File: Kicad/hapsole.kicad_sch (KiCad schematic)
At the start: 52 parts, among them J1 USB_C_Receptacle_USB2.0_16P, J2 Conn_01x02_Socket, J3 Conn_01x02_Socket, Q1 PMOS, U1 DA7280-00V42, U2 DA7280-00V42, U3 nRF52840, U4 LSM6DS3TR-C, U5 BQ25100YFPR, U6 TLV73333PDBV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

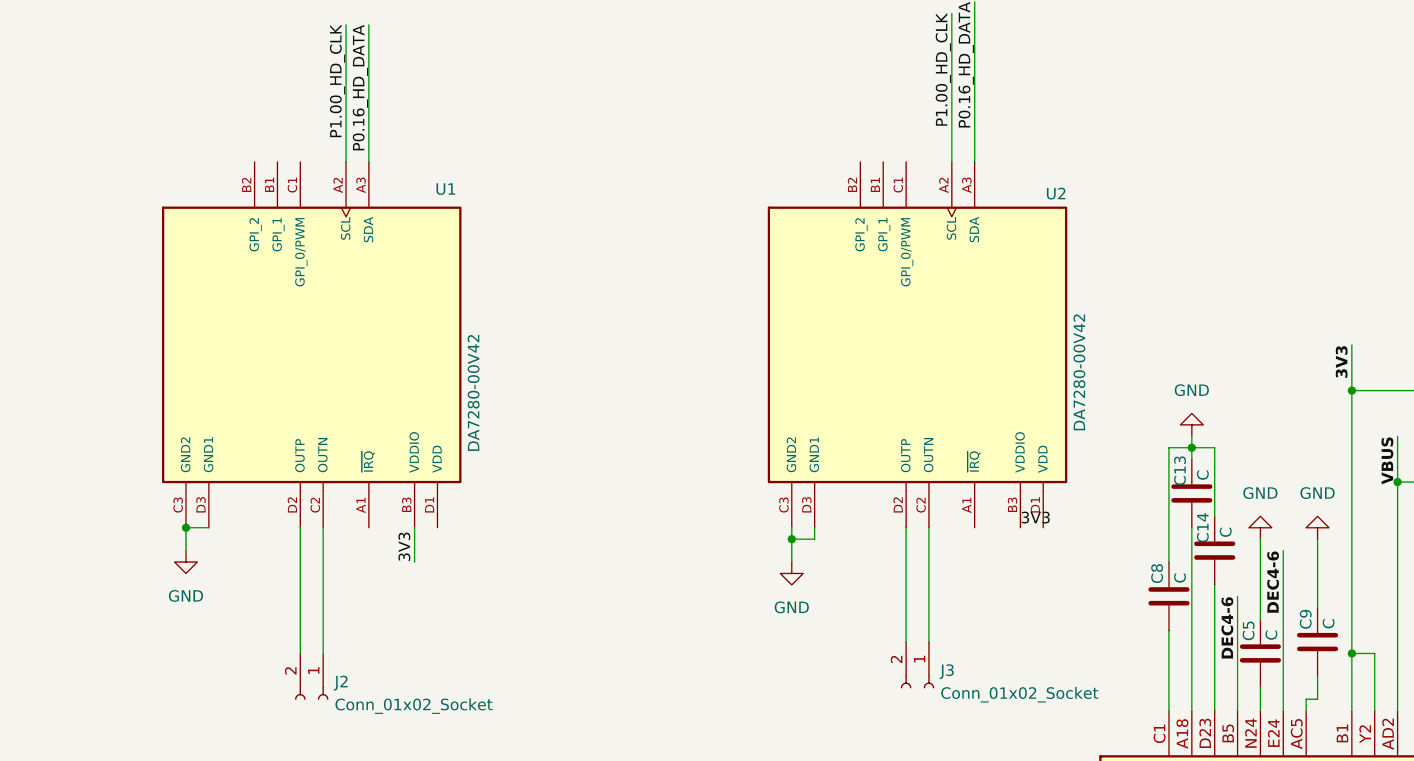
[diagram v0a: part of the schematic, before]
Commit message: added da7281
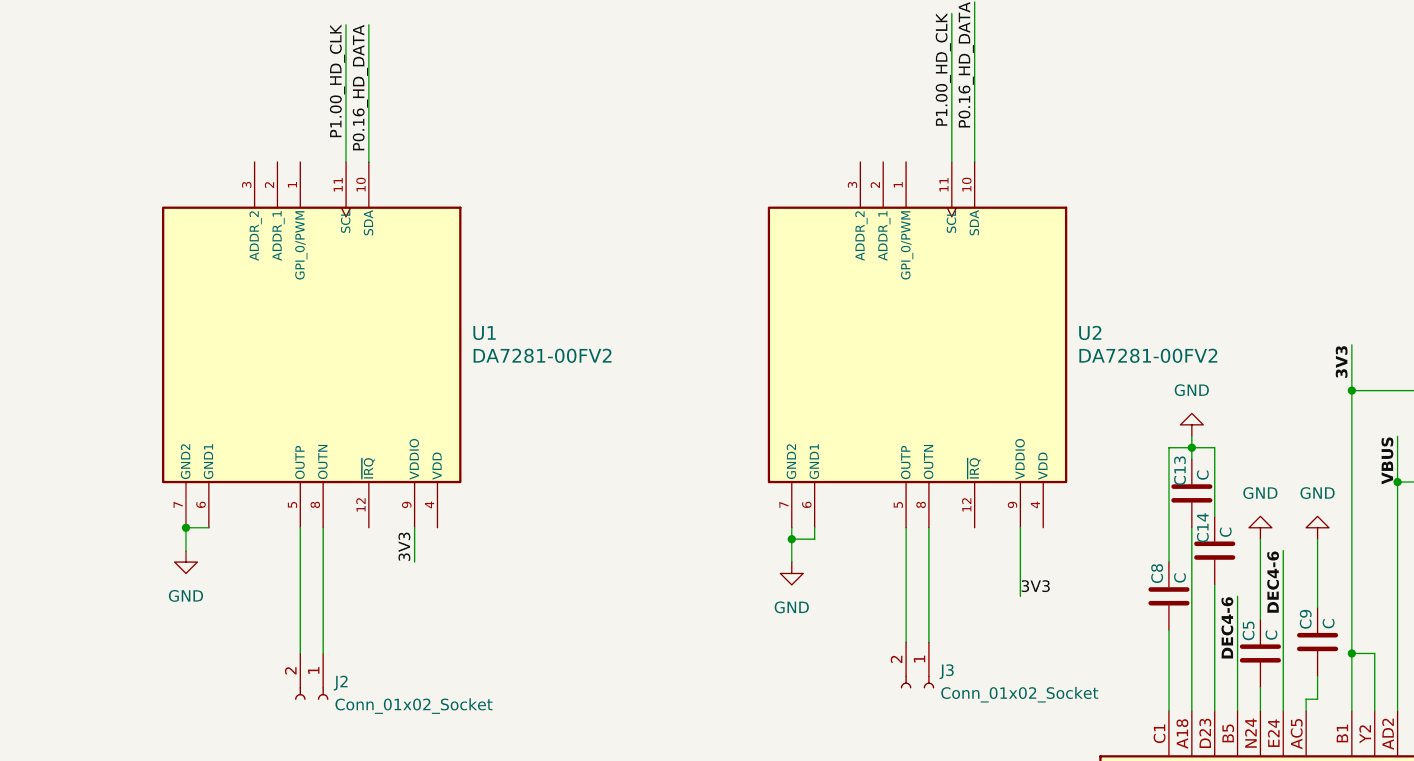
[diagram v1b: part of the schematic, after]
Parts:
- removed U1, U2: DA7280-00V42, DA7280-00V42:BGA12N40P4X3_175X135X57, symbol Arjun_Custom:DA7280-00V42
- added U1, U2: DA7281-00FV2, DA7281-00FV2_DIL, symbol Arjun_Custom:DA7281-00FV2
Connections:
- net 3V3: now also U1.9 (VDDIO), U2.9 (VDDIO)
- net GND: now also U1.6 (GND1), U1.7 (GND2), U2.6 (GND1), U2.7 (GND2)
- net P0.16_HD_DATA: now also U1.10 (SDA), U2.10 (SDA)
- net P1.00_HD_CLK: now also U1.11 (SCL), U2.11 (SCL)
- net at J3.1 (Pin_1): now also U2.8 (OUTN)
- net at J3.2 (Pin_2): now also U2.5 (OUTP)
- net at J2.1 (Pin_1): now also U1.8 (OUTN)
- net at J2.2 (Pin_2): now also U1.5 (OUTP)

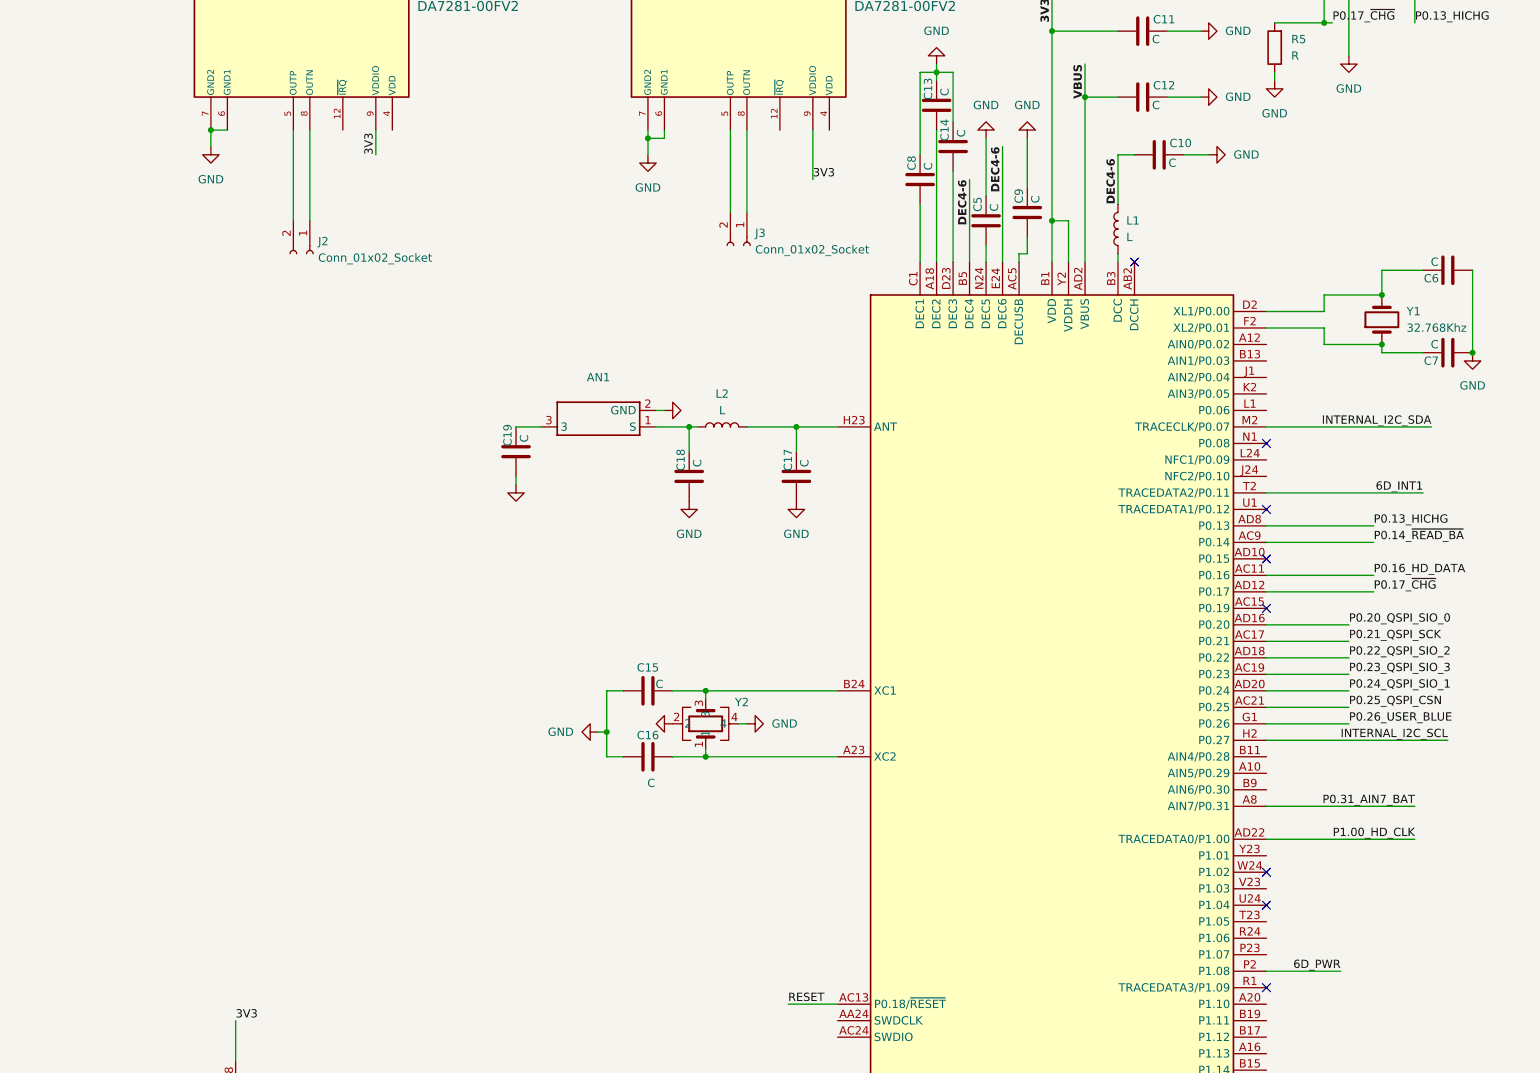
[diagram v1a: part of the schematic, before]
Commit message: Added Footprints of R,C
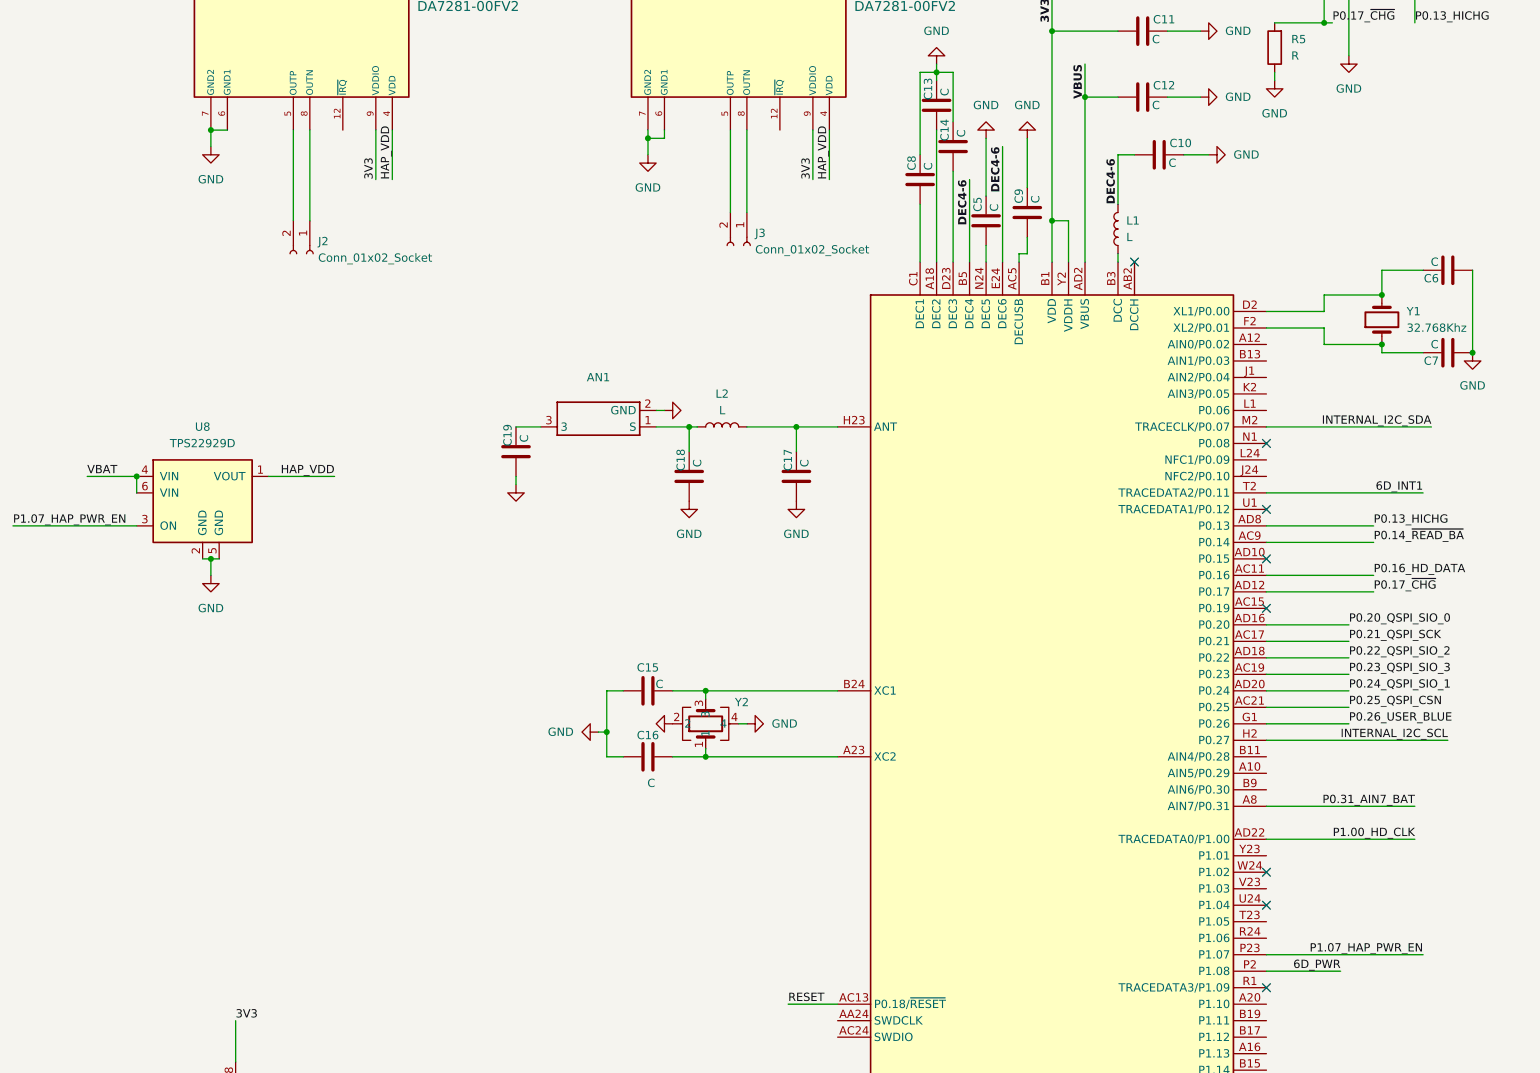
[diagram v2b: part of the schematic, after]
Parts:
- added U8: TPS22929D, Package_TO_SOT_SMD:SOT-23-6, symbol Power_Management:TPS22929D
- C1, C2: footprint (none) -> Capacitor_SMD:C_0402_1005Metric_Pad0.74x0.62mm_HandSolder
- C10, C11, C12, C13, C14, C15, C16, C17, C18, C19, C5, C6, C7, C8, C9: footprint (none) -> Capacitor_SMD:C_0402_1005Metric
- C3, C4: footprint (none) -> Capacitor_SMD:C_0603_1608Metric
- D1: footprint (none) -> Diode_SMD:D_0603_1608Metric
- L1, L2: footprint (none) -> Inductor_SMD:L_0402_1005Metric
- R1, R2, R3: footprint (none) -> Resistor_SMD:R_0603_1608Metric
- R10, R11, R12, R13, R4, R5, R6, R7, R8, R9: footprint (none) -> Resistor_SMD:R_0402_1005Metric_Pad0.72x0.64mm_HandSolder
- U1, U2: footprint DA7281-00FV2_DIL -> Arjun_Custom:DA7281-00FV2_DIL
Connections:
- net GND: now also U8.2 (GND), U8.5 (GND)
- net VBAT: now also U8.4 (VIN), U8.6 (VIN)
- net HAP_VDD: now reaches U2.4 (VDD)
- net HAP_VDD: now also U1.4 (VDD), U8.1 (VOUT)
- net P1.07_HAP_PWR_EN: now reaches U3.P23 (P1.07)
- net P1.07_HAP_PWR_EN: now also U8.3 (ON)

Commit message: initiated the PCB design
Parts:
- removed J1: USB_C_Receptacle_USB2.0_16P, symbol Connector:USB_C_Receptacle_USB2.0_16P
- added C20: 100n, Capacitor_SMD:C_0201_0603Metric, symbol Device:C
- added J1: 2171790001, Arjun_Custom:MOLEX_2171790001, symbol Arjun_Custom:2171790001
- added R14, R15, R16, R17, R18: 10k, Resistor_SMD:R_0201_0603Metric, symbol Device:R
- added SW1: SW_SPST, Arjun_Custom:SW_EVP-AWED4A, symbol Switch:SW_SPST
- added TP3, TP4, TP5, TP6: TestPoint, TestPoint:TestPoint_Pad_2.0x2.0mm, symbol Connector:TestPoint
- C1, C2: value C -> 2.2u; footprint Capacitor_SMD:C_0402_1005Metric_Pad0.74x0.62mm_HandSolder -> Capacitor_SMD:C_0201_0603Metric
- C10, C11, C12: value C -> 2.2u; footprint Capacitor_SMD:C_0402_1005Metric -> Capacitor_SMD:C_0201_0603Metric
- C13, C15, C16, C6, C7, C9: footprint Capacitor_SMD:C_0402_1005Metric -> Capacitor_SMD:C_0201_0603Metric
- C14: value C -> 100p; footprint Capacitor_SMD:C_0402_1005Metric -> Capacitor_SMD:C_0201_0603Metric
- C17, C18: value C -> 0.5p; footprint Capacitor_SMD:C_0402_1005Metric -> Capacitor_SMD:C_0201_0603Metric
- C19: value C -> 1n; footprint Capacitor_SMD:C_0402_1005Metric -> Capacitor_SMD:C_0201_0603Metric
- C3, C4: value C -> 2.2u; footprint Capacitor_SMD:C_0603_1608Metric -> Capacitor_SMD:C_0201_0603Metric
- C5: value C -> 820p; footprint Capacitor_SMD:C_0402_1005Metric -> Capacitor_SMD:C_0201_0603Metric
- C8: value C -> 100n; footprint Capacitor_SMD:C_0402_1005Metric -> Capacitor_SMD:C_0201_0603Metric
- J2, J3: footprint (none) -> Arjun_Custom:JST_S2B-PH-SM4-TB
- L1: value L -> 10u
- L2: value L -> 4.7n
- Q1: footprint (none) -> Package_TO_SOT_SMD:SOT-883
- R1: value R -> 5k1; footprint Resistor_SMD:R_0603_1608Metric -> Resistor_SMD:R_0201_0603Metric
- R10, R11, R9: value R -> 2.2k; footprint Resistor_SMD:R_0402_1005Metric_Pad0.72x0.64mm_HandSolder -> Resistor_SMD:R_0201_0603Metric
- R12, R13: value R -> 33R; footprint Resistor_SMD:R_0402_1005Metric_Pad0.72x0.64mm_HandSolder -> Resistor_SMD:R_0201_0603Metric
- R2: value R -> 1M_1%; footprint Resistor_SMD:R_0603_1608Metric -> Resistor_SMD:R_0201_0603Metric
- R3: value R -> 510k_1%; footprint Resistor_SMD:R_0603_1608Metric -> Resistor_SMD:R_0201_0603Metric
- R4: value R -> 10k; footprint Resistor_SMD:R_0402_1005Metric_Pad0.72x0.64mm_HandSolder -> Resistor_SMD:R_0201_0603Metric
- R5, R8: footprint Resistor_SMD:R_0402_1005Metric_Pad0.72x0.64mm_HandSolder -> Resistor_SMD:R_0201_0603Metric
- R6, R7: value R -> 2.7k; footprint Resistor_SMD:R_0402_1005Metric_Pad0.72x0.64mm_HandSolder -> Resistor_SMD:R_0201_0603Metric
- TP1, TP2: footprint (none) -> TestPoint:TestPoint_Pad_D3.0mm
- U5: footprint BQ25100YFPR:BGA6N40P3X2_157X88X50N -> Arjun_Custom:BGA6N40P3X2_157X88X50N
- Y1: footprint (none) -> Arjun_Custom:XTAL_FC-135_32.7680KA-A0
- Y2: footprint (none) -> Arjun_Custom:XTAL_ABM12W-40.0000MHZ-6-D1X-T3
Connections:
- net P0.14_~{READ_BA} is gone; now on net P0.14_~{READ_BAT}: U3.AC9 (P0.14)
- net P0.21_QSPI_SIO_3 is gone; now on net P0.23_QSPI_SIO_3: U7.7 (~{HOLD}/~{RESET}/IO_{3})
- net P0.26_USER_GREEN is gone; now on net P0.28_USER_GREEN: R11.1
- net 3V3: now also U2.2 (ADDR_1), U2.3 (ADDR_2), R16.1, R17.2, R18.2
- net 6D_PWR: now also R14.2, R15.2
- net GND: now also R1.1, U1.2 (ADDR_1), U1.3 (ADDR_2), C20.2, J1.A1B12 (GND1), J1.B1A12 (GND2), SW1.2 (B), TP3.1; no longer R1.2
- net INTERNAL_I2C_SCL: now also R14.1
- net INTERNAL_I2C_SDA: now also R15.1
- net P0.16_HD_DATA: now also R18.1
- net P1.00_HD_CLK: now also R17.1
- net RESET: now also C20.1, R16.2, SW1.1 (A), TP4.1
- net USB_D+: now also J1.A6 (DP1), J1.B6 (DP2)
- net USB_D-: now also J1.A7 (DN1), J1.B7 (DN2)
- net VBUS: now also J1.A4B9 (VBUS1), J1.B4A9 (VBUS2)
- net P0.04_da7281_pwm_2: now reaches U2.1 (GPI_0/PWM)
- net P0.04_da7281_pwm_2: now also U3.J1 (AIN2/P0.04)
- net P0.12_da7281_IRQ_2: now reaches U2.12 (~{IRQ})
- net P0.12_da7281_IRQ_2: now also U3.N1 (P0.08)
- net P0.03_da7281_pwm_1: now reaches U1.1 (GPI_0/PWM)
- net P0.03_da7281_pwm_1: now also U3.B13 (AIN1/P0.03)
- net P0.12_da7281_IRQ_1: now reaches U1.12 (~{IRQ})
- net P0.12_da7281_IRQ_1: now also U3.U1 (TRACEDATA1/P0.12)
- net SWDCLK: now reaches U3.AA24 (SWDCLK)
- net SWDCLK: now also TP5.1
- net SWDIO: now reaches U3.AC24 (SWDIO)
- net SWDIO: now also TP6.1
- net P0.28_USER_GREEN: now reaches U3.B11 (AIN4/P0.28)
- new net: J1.A5 (CC1), R1.2
- no-connect marks 11 -> 31
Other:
- moved on the sheet: C3, C4, C7, J2, J3, R1, U4

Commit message: placed the components in PCB & started routing
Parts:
- removed D2: Inolux_IN-P55TATRGB, LED_SMD:LED_Inolux_IN-P55TATRGB_PLCC6_5.0x5.5mm_P1.8mm, symbol LED:Inolux_IN-P55TATRGB
- added LED1: ~, Arjun_Custom:RGB_LED_P4_1010, symbol Arjun_Custom:RGB_LED_P4_1010
- AN1: footprint (none) -> Arjun_Custom:Ant
- J2, J3: footprint Arjun_Custom:JST_S2B-PH-SM4-TB -> Arjun_Custom:JST_S2B-ZR-SM4A-TF
- TP1, TP2: footprint TestPoint:TestPoint_Pad_D3.0mm -> TestPoint:TestPoint_Pad_D1.5mm
- TP3, TP4, TP5, TP6: footprint TestPoint:TestPoint_Pad_2.0x2.0mm -> TestPoint:TestPoint_Pad_1.0x1.0mm
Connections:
- net 3V3: now also LED1.+
- net at R9.2: now also LED1.B-
- net at U2.5 (OUTP): now also J3.1 (Pin_1); no longer J3.2 (Pin_2)
- net at U2.8 (OUTN): now also J3.2 (Pin_2); no longer J3.1 (Pin_1)
- net at R11.2: now also LED1.R-
- net at R10.2: now also LED1.G-
- net at U1.5 (OUTP): now also J2.1 (Pin_1); no longer J2.2 (Pin_2)
- net at U1.8 (OUTN): now also J2.2 (Pin_2); no longer J2.1 (Pin_1)
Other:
- moved on the sheet: J2, J3

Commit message: added library
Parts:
- U3: footprint Package_DFN_QFN:Nordic_AQFN-73-1EP_7x7mm_P0.5mm -> Arjun_Custom:NRF52840
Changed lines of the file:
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@@
 			)
 		)
-		(property "Footprint" "Package_DFN_QFN:Nordic_AQFN-73-1EP_7x7mm_P0.5mm"
+		(property "Footprint" "Arjun_Custom:NRF52840"
 			(at 175.26 252.73 0)
 			(effects
